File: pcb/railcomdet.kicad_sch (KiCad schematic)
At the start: 43 parts, among them J1 MVE252-5-V, J10 MVE252-5-V, J2 MVE252-5-V, J3 MVE252-5-V, J4 MVE252-5-V, J5 MVE252-5-V, J9 MVE252-5-V, U1 VO0631T, U2 VO0631T, U3 VO0631T

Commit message: Use handsolder SMDs where possible.
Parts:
- C1, C2, C3, C4: footprint Capacitor_SMD:C_0805_2012Metric -> Capacitor_SMD:C_0805_2012Metric_Pad1.18x1.45mm_HandSolder
- R1, R10, R11, R12, R13, R2, R3, R4, R5, R6, R7, R8, R9: footprint Resistor_SMD:R_0805_2012Metric -> Resistor_SMD:R_0805_2012Metric_Pad1.20x1.40mm_HandSolder
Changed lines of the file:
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@@
       (effects (font (size 1.27 1.27)))
     )
-    (property "Footprint" "Resistor_SMD:R_0805_2012Metric" (at 162.56 105.918 90)
+    (property "Footprint" "Resistor_SMD:R_0805_2012Metric_Pad1.20x1.40mm_HandSolder" (at 162.56 105.918 90)
       (effects (font (size 1.27 1.27)) hide)
     )
@@
       (effects (font (size 1.27 1.27)) (justify left))
     )
-    (property "Footprint" "Capacitor_SMD:C_0805_2012Metric" (at 194.0052 30.48 0)
+    (property "Footprint" "Capacitor_SMD:C_0805_2012Metric_Pad1.18x1.45mm_HandSolder" (at 194.0052 30.48 0)
       (effects (font (size 1.27 1.27)) hide)
     )
@@
       (effects (font (size 1.27 1.27)) (justify left))
     )
-    (property "Footprint" "Resistor_SMD:R_0805_2012Metric" (at 128.778 96.52 90)
+    (property "Footprint" "Resistor_SMD:R_0805_2012Metric_Pad1.20x1.40mm_HandSolder" (at 128.778 96.52 90)
       (effects (font (size 1.27 1.27)) hide)
     )
@@
       (effects (font (size 1.27 1.27)) (justify left))
     )
-    (property "Footprint" "Resistor_SMD:R_0805_2012Metric" (at 169.672 63.5 90)
+    (property "Footprint" "Resistor_SMD:R_0805_2012Metric_Pad1.20x1.40mm_HandSolder" (at 169.672 63.5 90)
       (effects (font (size 1.27 1.27)) hide)
     )
@@
       (effects (font (size 1.27 1.27)) (justify left))
     )
-    (property "Footprint" "Capacitor_SMD:C_0805_2012Metric" (at 102.5652 30.48 0)
+    (property "Footprint" "Capacitor_SMD:C_0805_2012Metric_Pad1.18x1.45mm_HandSolder" (at 102.5652 30.48 0)
       (effects (font (size 1.27 1.27)) hide)
     )
@@
       (effects (font (size 1.27 1.27)) (justify left))
     )
-    (property "Footprint" "Resistor_SMD:R_0805_2012Metric" (at 119.888 106.68 90)
+    (property "Footprint" "Resistor_SMD:R_0805_2012Metric_Pad1.20x1.40mm_HandSolder" (at 119.888 106.68 90)
       (effects (font (size 1.27 1.27)) hide)
     )
@@
       (effects (font (size 1.27 1.27)))
     )
-    (property "Footprint" "Resistor_SMD:R_0805_2012Metric" (at 127 67.818 90)
+    (property "Footprint" "Resistor_SMD:R_0805_2012Metric_Pad1.20x1.40mm_HandSolder" (at 127 67.818 90)
       (effects (font (size 1.27 1.27)) hide)
     )
@@
       (effects (font (size 1.27 1.27)) (justify left))
     )
-    (property "Footprint" "Resistor_SMD:R_0805_2012Metric" (at 160.782 53.34 90)
+    (property "Footprint" "Resistor_SMD:R_0805_2012Metric_Pad1.20x1.40mm_HandSolder" (at 160.782 53.34 90)
       (effects (font (size 1.27 1.27)) hide)
     )
@@
       (effects (font (size 1.27 1.27)))
     )
-    (property "Footprint" "Resistor_SMD:R_0805_2012Metric" (at 125.73 149.098 90)
+    (property "Footprint" "Resistor_SMD:R_0805_2012Metric_Pad1.20x1.40mm_HandSolder" (at 125.73 149.098 90)
       (effects (font (size 1.27 1.27)) hide)
     )
@@
       (effects (font (size 1.27 1.27)) (justify left))
     )
-    (property "Footprint" "Capacitor_SMD:C_0805_2012Metric" (at 180.0352 30.48 0)
+    (property "Footprint" "Capacitor_SMD:C_0805_2012Metric_Pad1.18x1.45mm_HandSolder" (at 180.0352 30.48 0)
       (effects (font (size 1.27 1.27)) hide)
     )
@@
       (effects (font (size 1.27 1.27)))
     )
-    (property "Footprint" "Resistor_SMD:R_0805_2012Metric" (at 125.73 144.018 90)
+    (property "Footprint" "Resistor_SMD:R_0805_2012Metric_Pad1.20x1.40mm_HandSolder" (at 125.73 144.018 90)
       (effects (font (size 1.27 1.27)) hide)
     )
@@
       (effects (font (size 1.27 1.27)) (justify left))
     )
-    (property "Footprint" "Resistor_SMD:R_0805_2012Metric" (at 189.992 133.35 90)
+    (property "Footprint" "Resistor_SMD:R_0805_2012Metric_Pad1.20x1.40mm_HandSolder" (at 189.992 133.35 90)
       (effects (font (size 1.27 1.27)) hide)
     )
@@
       (effects (font (size 1.27 1.27)))
     )
-    (property "Footprint" "Resistor_SMD:R_0805_2012Metric" (at 127 62.738 90)
+    (property "Footprint" "Resistor_SMD:R_0805_2012Metric_Pad1.20x1.40mm_HandSolder" (at 127 62.738 90)
       (effects (font (size 1.27 1.27)) hide)
     )
@@
       (effects (font (size 1.27 1.27)) (justify left))
     )
-    (property "Footprint" "Resistor_SMD:R_0805_2012Metric" (at 168.402 144.78 90)
+    (property "Footprint" "Resistor_SMD:R_0805_2012Metric_Pad1.20x1.40mm_HandSolder" (at 168.402 144.78 90)
       (effects (font (size 1.27 1.27)) hide)
     )
@@
       (effects (font (size 1.27 1.27)))
     )
-    (property "Footprint" "Resistor_SMD:R_0805_2012Metric" (at 162.56 110.998 90)
+    (property "Footprint" "Resistor_SMD:R_0805_2012Metric_Pad1.20x1.40mm_HandSolder" (at 162.56 110.998 90)
       (effects (font (size 1.27 1.27)) hide)
     )
@@
       (effects (font (size 1.27 1.27)) (justify left))
     )
-    (property "Footprint" "Capacitor_SMD:C_0805_2012Metric" (at 192.7352 148.59 0)
+    (property "Footprint" "Capacitor_SMD:C_0805_2012Metric_Pad1.18x1.45mm_HandSolder" (at 192.7352 148.59 0)
       (effects (font (size 1.27 1.27)) hide)
     )
@@
       (effects (font (size 1.27 1.27)))
     )
-    (property "Footprint" "Resistor_SMD:R_0805_2012Metric" (at 180.34 137.922 90)
-      (effects (font (size 1.27 1.27)) hide)
-    )
+    (property "Footprint" "Resistor_SMD:R_0805_2012Metric_Pad1.20x1.40mm_HandSolder" (at 180.34 137.922 90)
+      (effects (font (size 1.27 1.27)) hide)
+    )

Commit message: Pcb tweaks.
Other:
- title: RailComDet - root -> MTB-RC - MTBbus RailCom detector - root schematic
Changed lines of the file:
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@@
   (paper "A4")
   (title_block
-    (title "RailComDet - root")
+    (title "MTB-RC - MTBbus RailCom detector - root schematic")
     (date "2023-10-23")
     (rev "1.0")

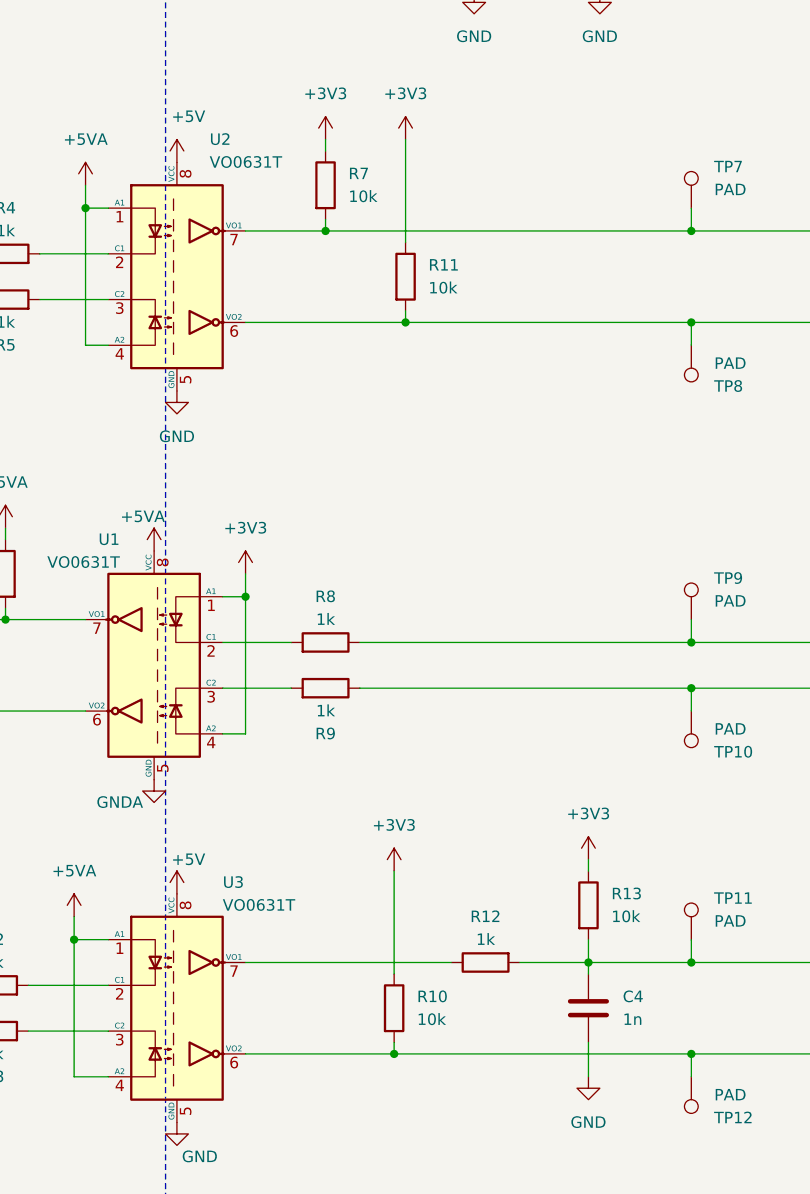
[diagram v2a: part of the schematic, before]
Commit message: Use smaller pull-ups for RailCom RX.
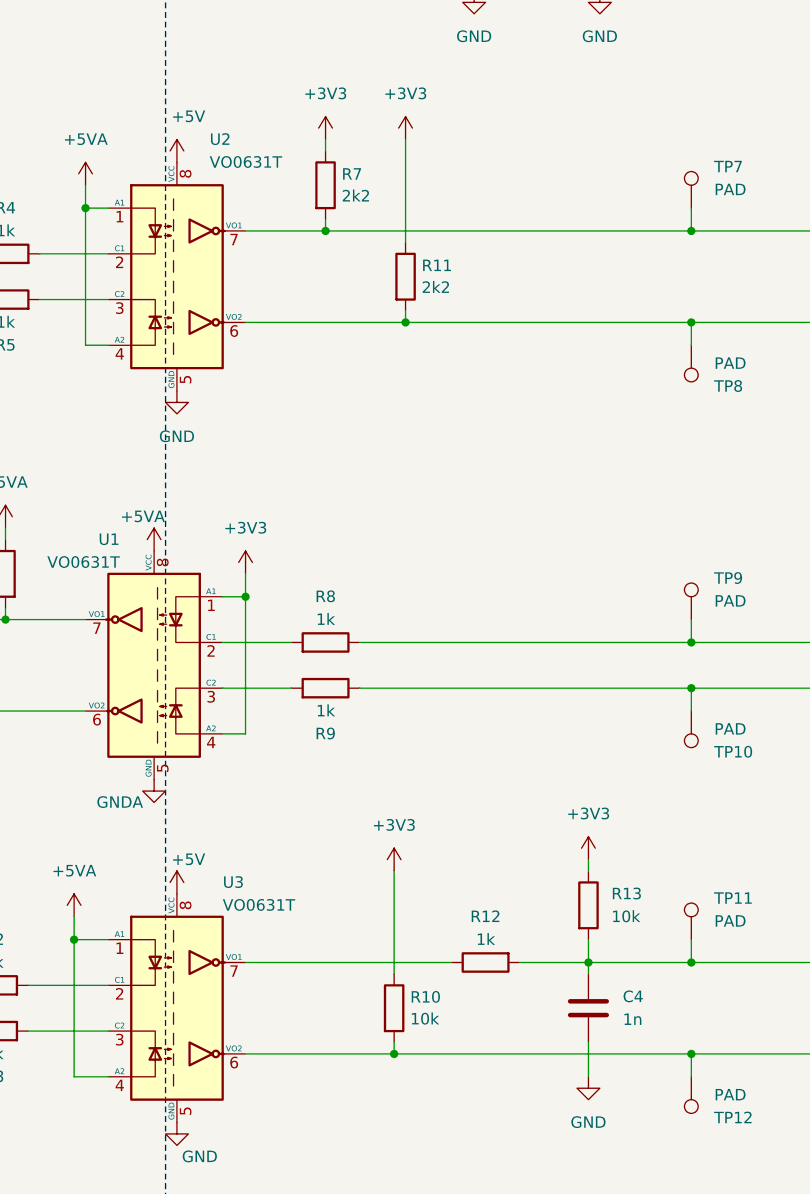
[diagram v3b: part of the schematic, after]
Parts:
- R11, R7: value 10k -> 2k2
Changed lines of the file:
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@@
   (symbol (lib_id "Device:R") (at 171.45 63.5 0) (unit 1)
     (in_bom yes) (on_board yes) (dnp no) (fields_autoplaced)
-    (property "Reference" "R11" (at 173.99 62.23 0)
-      (effects (font (size 1.27 1.27)) (justify left))
-    )
-    (property "Value" "10k" (at 173.99 64.77 0)
+    (property "Reference" "R11" (at 173.228 62.2879 0)
+      (effects (font (size 1.27 1.27)) (justify left))
+    )
+    (property "Value" "2k2" (at 173.228 64.7121 0)
       (effects (font (size 1.27 1.27)) (justify left))
     )
@@
   (symbol (lib_id "Device:R") (at 162.56 53.34 0) (unit 1)
     (in_bom yes) (on_board yes) (dnp no) (fields_autoplaced)
-    (property "Reference" "R7" (at 165.1 52.07 0)
-      (effects (font (size 1.27 1.27)) (justify left))
-    )
-    (property "Value" "10k" (at 165.1 54.61 0)
+    (property "Reference" "R7" (at 164.338 52.1279 0)
+      (effects (font (size 1.27 1.27)) (justify left))
+    )
+    (property "Value" "2k2" (at 164.338 54.5521 0)
       (effects (font (size 1.27 1.27)) (justify left))
     )
@@
   (symbol (lib_id "Device:R") (at 170.18 144.78 0) (unit 1)
     (in_bom yes) (on_board yes) (dnp no) (fields_autoplaced)
-    (property "Reference" "R10" (at 172.72 143.51 0)
-      (effects (font (size 1.27 1.27)) (justify left))
-    )
-    (property "Value" "10k" (at 172.72 146.05 0)
-      (effects (font (size 1.27 1.27)) (justify left))
-    )
+    (property "Reference" "R10" (at 171.958 143.5679 0)
+      (effects (font (size 1.27 1.27)) (justify left))
+    )
+    (property "Value" "10k" (at 171.958 145.9921 0)
+      (effects (font (size 1.27 1.27)) (justify left))
+    )

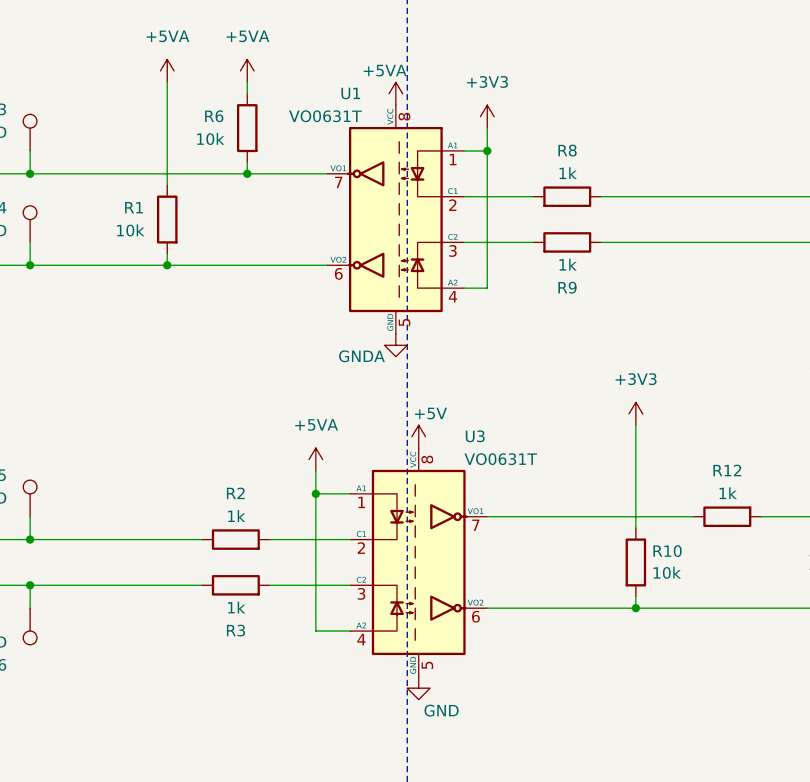
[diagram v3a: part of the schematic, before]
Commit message: Tweak optocoupler LED current.
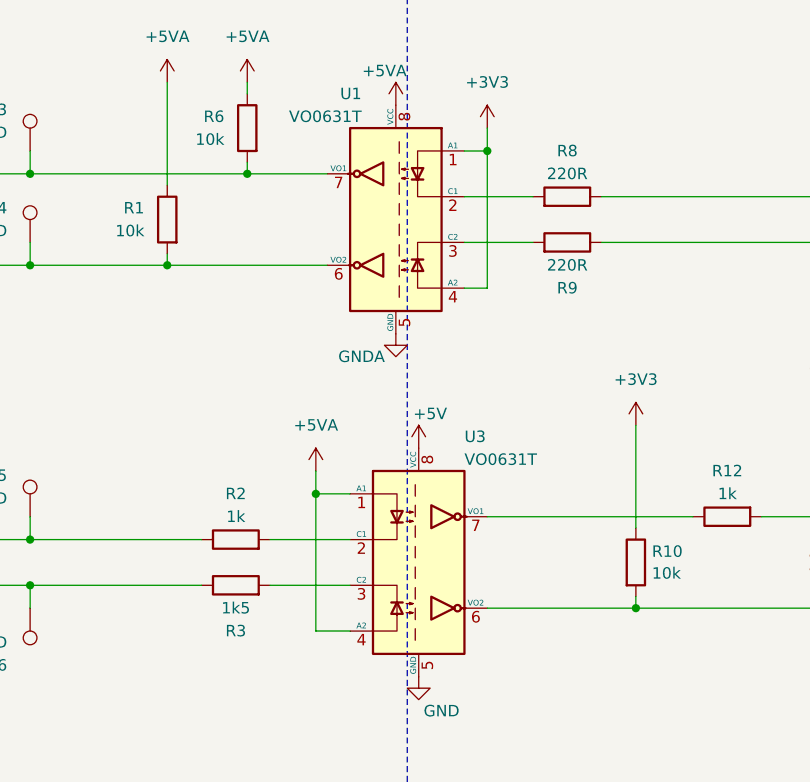
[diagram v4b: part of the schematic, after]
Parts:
- R3: value 1k -> 1k5
- R8, R9: value 1k -> 220R
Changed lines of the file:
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@@
       (effects (font (size 1.27 1.27)))
     )
-    (property "Value" "1k" (at 162.56 101.6 90)
+    (property "Value" "220R" (at 162.56 101.6 90)
       (effects (font (size 1.27 1.27)))
     )
@@
       (effects (font (size 1.27 1.27)))
     )
-    (property "Value" "1k" (at 125.73 149.86 90)
+    (property "Value" "1k5" (at 125.73 149.86 90)
       (effects (font (size 1.27 1.27)))
     )
@@
       (effects (font (size 1.27 1.27)))
     )
-    (property "Value" "1k" (at 162.56 111.76 90)
-      (effects (font (size 1.27 1.27)))
-    )
+    (property "Value" "220R" (at 162.56 111.76 90)
+      (effects (font (size 1.27 1.27)))
+    )

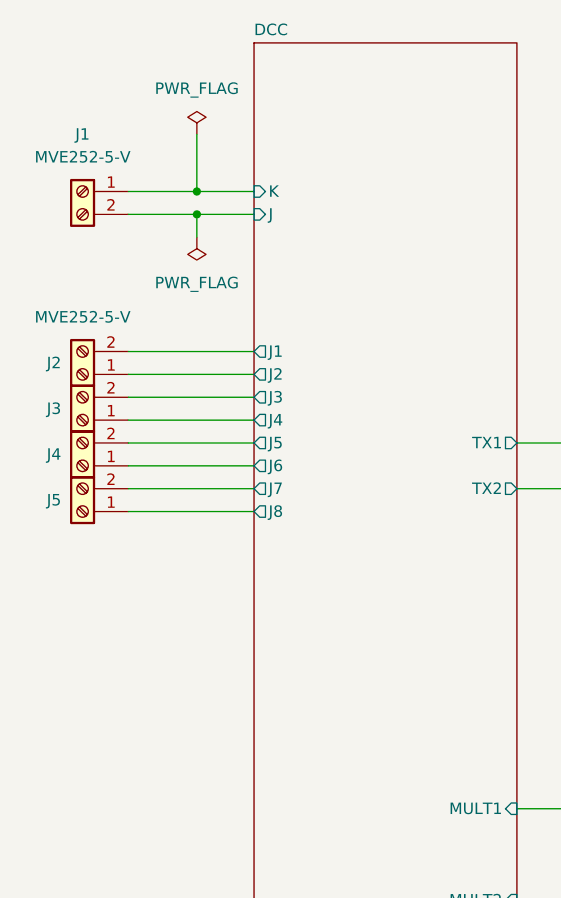
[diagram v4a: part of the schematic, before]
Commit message: Use double J & K connectors.
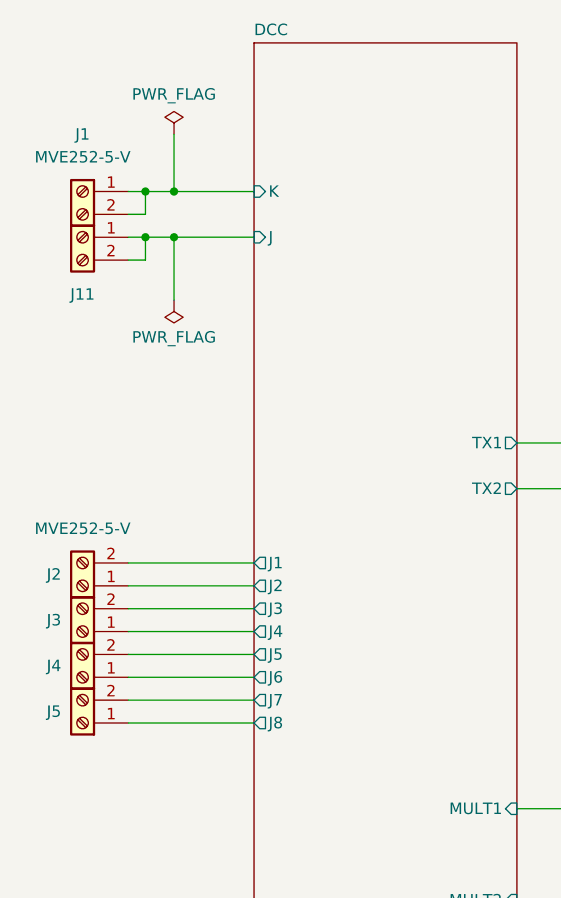
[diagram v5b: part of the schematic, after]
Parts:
- added J11: MVE252-5-V, TerminalBlock_Euroclamp:MVE252-5-V, symbol Connector:Screw_Terminal_01x02
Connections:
- net DCC/J: now also J11.1 (Pin_1), J11.2 (Pin_2); no longer J1.2 (Pin_2)
- net DCC/K: now also J1.2 (Pin_2)
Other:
- moved on the sheet: J2, J3, J4, J5
